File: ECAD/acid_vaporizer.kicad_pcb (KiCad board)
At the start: 2 copper layers, 98 x 50 mm, 66 parts, among them J1 Screw_Terminal_01x02, J2 Screw_Terminal_01x02, J3 Screw_Terminal_01x01, J4 Screw_Terminal_01x01, J5 Conn_ARM_JTAG_SWD_10, J6 Screw_Terminal_01x02, J7 Conn_01x02_Male, Q1 BTA16-800BW, Q2 BC817, Q3 BC817, Q4 BC817, U1 OPA333xxD, U2 STM32F030F4Px, U3 AMS1117-3.3, U4 OPA333xxD, U5 DS18B20, U6 74HC164, U7 MOC3063M, U8 E30281, Y1 8MHz

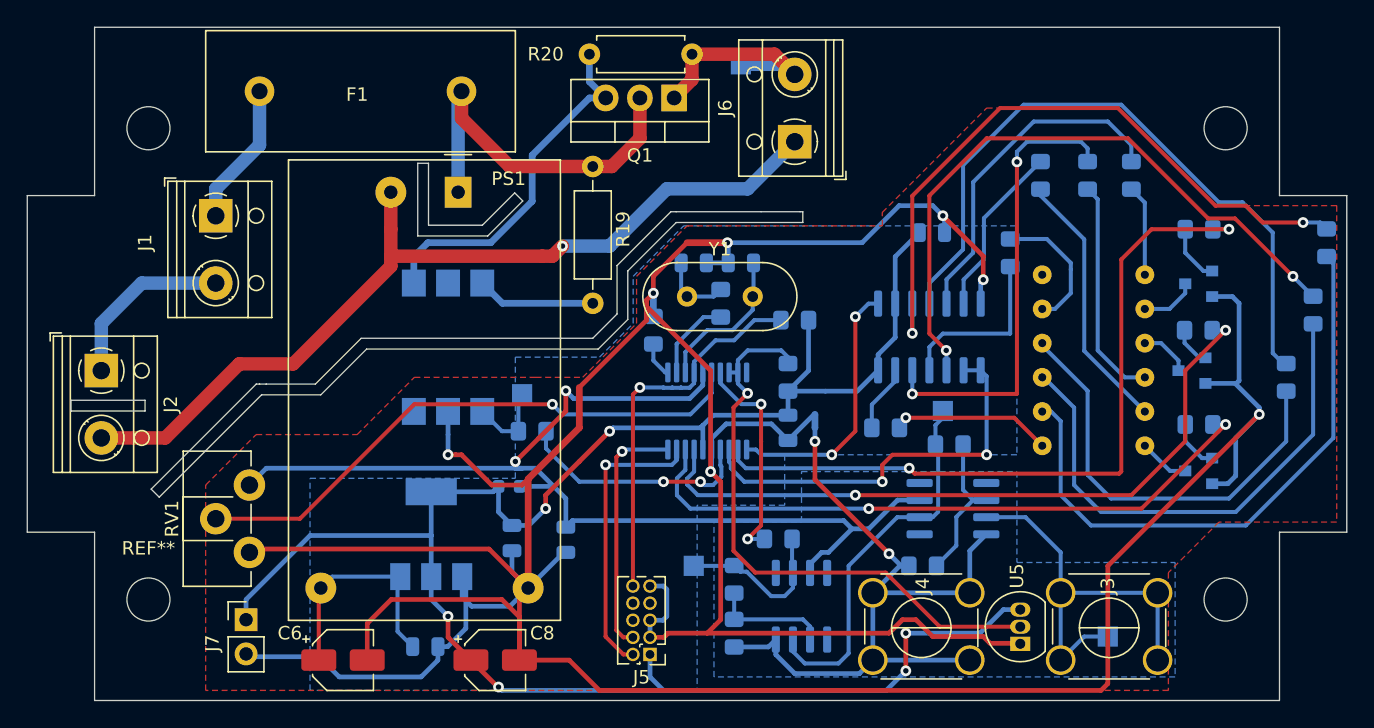
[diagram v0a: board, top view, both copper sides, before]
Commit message: Schematic and PCB: replasce DS18B20 by TMP36
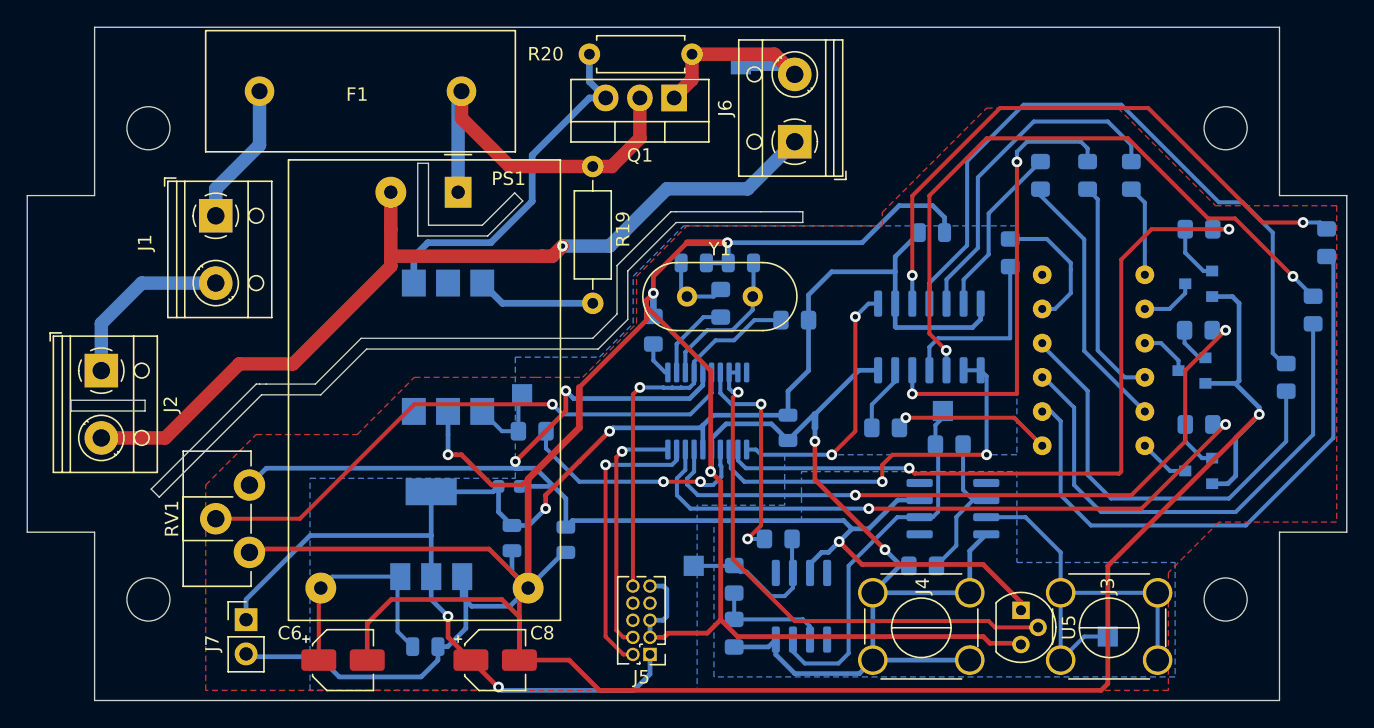
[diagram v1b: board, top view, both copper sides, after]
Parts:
- removed R9: 3K3, Resistor_SMD:R_0805_2012Metric_Pad1.15x1.40mm_HandSolder
- removed the REF** at (139.0, 98.0)
- removed the REF** at (139.0, 133.0)
- removed the REF** at (59.0, 98.0)
- added REF**: MountingHole_3.2mm_M3_DIN965, MountingHole:MountingHole_3.2mm_M3_DIN965, F.Cu at (139.0, 133.0)
- added REF**: MountingHole_3.2mm_M3_DIN965, MountingHole:MountingHole_3.2mm_M3_DIN965, F.Cu at (59.0, 98.0)
- added REF**: MountingHole_3.2mm_M3_DIN965, MountingHole:MountingHole_3.2mm_M3_DIN965, F.Cu at (139.0, 98.0)
- U5: value DS18B20 -> TMP36xT; footprint Package_TO_SOT_THT:TO-92_Inline -> Package_TO_SOT_THT:TO-92
- moved U5 2.49 mm to (123.8, 133.8), turned to 270 degrees
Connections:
- U5 pad 1: GND -> +3.3VA
- U5 pad 3: +3V3 -> GND
- U6 pad 14: GND -> +3V3
- U6 pad 7: +3V3 -> GND
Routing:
- net +3V3: track 141.1 -> 114.1 mm, vias 6 -> 4
- net +3.3VA: track 81.7 -> 97.6 mm, vias 2 -> 3
- net Net-(R14-Pad2): track 49.6 -> 45.2 mm
- net Net-(U2-Pad8): track 43.9 -> 40.0 mm
- net GND: track 322.9 -> 319.7 mm, vias 7 -> 5
